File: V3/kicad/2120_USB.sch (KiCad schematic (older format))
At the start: 5 parts, among them J2120 USB_B, J2121 Conn_01x03_Male, U2120 MCP2221AxP

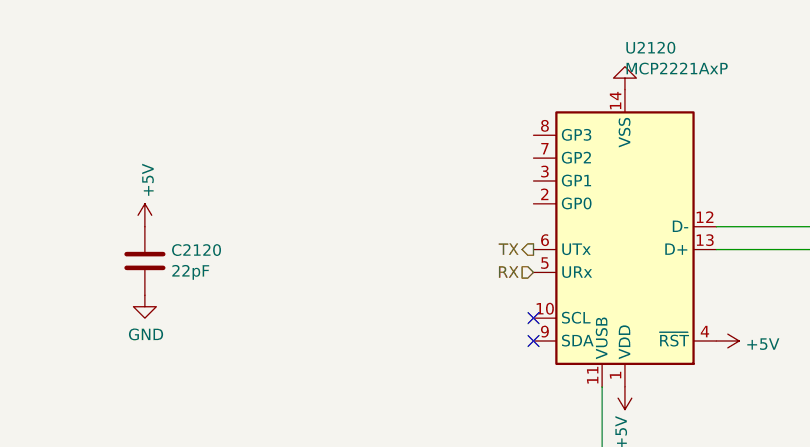
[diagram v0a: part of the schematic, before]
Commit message: Fixed a few USB/UART issues
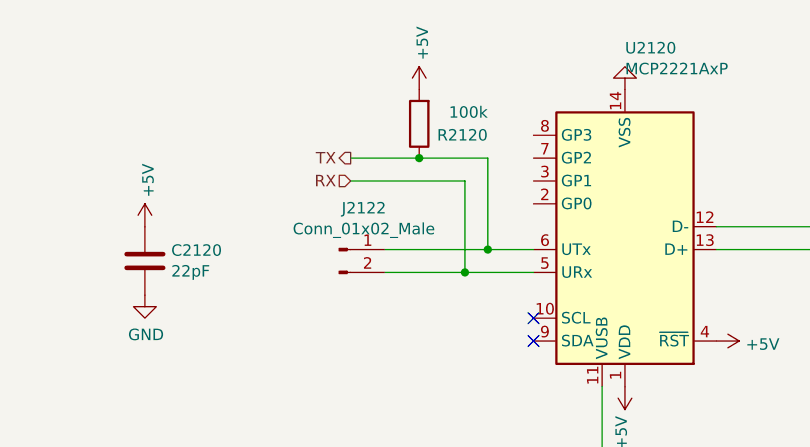
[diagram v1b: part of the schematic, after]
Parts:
- added J2122: Conn_01x02_Male, Connector_PinHeader_2.54mm:PinHeader_1x02_P2.54mm_Vertical, symbol Connector:Conn_01x02_Male
- added R2120: 100k, Resistor_THT:R_Axial_DIN0309_L9.0mm_D3.2mm_P2.54mm_Vertical, symbol Device:R
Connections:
- net +5V: now also R2120.2
- net RX: now also J2122.2 (Pin_2)
- net TX: now also J2122.1 (Pin_1), R2120.1
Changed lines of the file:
@@
 NoConn ~ 4650 4300
 NoConn ~ 4650 4400
-Text HLabel 4650 4000 0    50   Output ~ 0
-TX
-Text HLabel 4650 4100 0    50   Input ~ 0
-RX
 $Comp
 L Connector:Conn_01x03_Male J?
@@
 	1    0    0    -1
 $EndComp
+$Comp
+L Connector:Conn_01x02_Male J2122
+U 1 1 627627D6
+P 3800 4000
+F 0 "J2122" H 3908 4181 50  0000 C CNN
+F 1 "Conn_01x02_Male" H 3908 4090 50  0000 C CNN
+F 2 "Connector_PinHeader_2.54mm:PinHeader_1x02_P2.54mm_Vertical" H 3800 4000 50  0001 C CNN
+F 3 "~" H 3800 4000 50  0001 C CNN
+	1    3800 4000
+	1    0    0    -1
+$EndComp
+Wire Wire Line
+	3850 3600 4150 3600
+Wire Wire Line
+	3850 3700 4350 3700
+$Comp
+L power:+5V #PWR?
+U 1 1 6278A36E
+P 4150 3300
+AR Path="/6191B6A2/61EBDADB/6278A36E" Ref="#PWR?"  Part="1"
+AR Path="/6191B6A2/61EBDADB/62542978/6278A36E" Ref="#PWR0145"  Part="1"
+F 0 "#PWR0145" H 4150 3150 50  0001 C CNN
+F 1 "+5V" V 4165 3428 50  0000 L CNN
+F 2 "" H 4150 3300 50  0001 C CNN
+F 3 "" H 4150 3300 50  0001 C CNN
+	1    4150 3300
+	1    0    0    -1
+$EndComp
+$Comp
+L Device:R R2120
+U 1 1 6278730B
+P 4150 3450
+F 0 "R2120" H 3850 3500 50  0000 L CNN
+F 1 "100k" H 3850 3400 50  0000 L CNN
+F 2 "Resistor_THT:R_Axial_DIN0309_L9.0mm_D3.2mm_P2.54mm_Vertical" V 4080 3450 50  0001 C CNN
+F 3 "~" H 4150 3450 50  0001 C CNN
+	1    4150 3450
+	-1   0    0    1
+$EndComp
+Wire Wire Line
+	4450 3600 4450 4000
+Wire Wire Line
+	4450 4000 4650 4000
+Connection ~ 4450 4000
+Wire Wire Line
+	4450 4000 4000 4000
+Wire Wire Line
+	4650 4100 4350 4100
+Wire Wire Line
+	4000 4100 4350 4100
+Connection ~ 4350 4100
+Wire Wire Line
+	4350 3700 4350 4100
+Text HLabel 3850 3600 0    50   Output ~ 0
+TX
+Text HLabel 3850 3700 0    50   Input ~ 0
+RX
+Connection ~ 4150 3600
+Wire Wire Line
+	4150 3600 4450 3600
 $EndSCHEMATC

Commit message: Still putting final touches on CPU page
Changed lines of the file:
@@
 U 1 1 627627D6
 P 3800 4000
-F 0 "J2122" H 3908 4181 50  0000 C CNN
-F 1 "Conn_01x02_Male" H 3908 4090 50  0000 C CNN
+F 0 "J2122" H 3900 3800 50  0000 C CNN
+F 1 "Conn_01x02_Male" H 3900 3700 50  0000 C CNN
 F 2 "Connector_PinHeader_2.54mm:PinHeader_1x02_P2.54mm_Vertical" H 3800 4000 50  0001 C CNN
 F 3 "~" H 3800 4000 50  0001 C CNN

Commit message: Final checks and DRC
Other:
- note added: "This page has been checked!"
- note removed: "This page has NOT been checked!"
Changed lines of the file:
@@
 Connection ~ 6150 4200
 Text Notes 1250 6500 0    197  ~ 39
-This page has NOT been checked!
+This page has been checked!
 $Comp
 L Device:C C?

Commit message: Design Rule Check
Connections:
- no-connect marks 2 -> 6
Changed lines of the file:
@@
 Wire Wire Line
 	4150 3600 4450 3600
+NoConn ~ 4650 3500
+NoConn ~ 4650 3600
+NoConn ~ 4650 3700
+NoConn ~ 4650 3800
 $EndSCHEMATC

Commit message: just totally redid the whole thing
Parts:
- removed J2121: Conn_01x03_Male, Connector_PinHeader_2.54mm:PinHeader_1x03_P2.54mm_Vertical, symbol Connector:Conn_01x03_Male
- C2120, C2121: footprint Capacitor_THT:C_Rect_L4.0mm_W2.5mm_P2.50mm -> Capacitor_SMD:C_1206_3216Metric
- R2120: footprint Resistor_THT:R_Axial_DIN0309_L9.0mm_D3.2mm_P2.54mm_Vertical -> Resistor_SMD:R_1206_3216Metric
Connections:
- net +5V: now also J2120.1 (VBUS)
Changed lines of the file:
@@
 $Descr A4 11693 8268
 encoding utf-8
-Sheet 9 9
+Sheet 8 8
 Title ""
 Date ""
@@
 L power:+5V #PWR?
 U 1 1 6254C2ED
-P 6150 4200
+P 6350 4200
 AR Path="/6191B6A2/61EBDADB/6254C2ED" Ref="#PWR?"  Part="1"
 AR Path="/6191B6A2/61EBDADB/62542978/6254C2ED" Ref="#PWR0133"  Part="1"
-F 0 "#PWR0133" H 6150 4050 50  0001 C CNN
-F 1 "+5V" V 6165 4328 50  0000 L CNN
-F 2 "" H 6150 4200 50  0001 C CNN
-F 3 "" H 6150 4200 50  0001 C CNN
-	1    6150 4200
+F 0 "#PWR0133" H 6350 4050 50  0001 C CNN
+F 1 "+5V" V 6365 4328 50  0000 L CNN
+F 2 "" H 6350 4200 50  0001 C CNN
+F 3 "" H 6350 4200 50  0001 C CNN
+	1    6350 4200
 	0    -1   -1   0
 $EndComp
@@
 NoConn ~ 4650 4300
 NoConn ~ 4650 4400
-$Comp
-L Connector:Conn_01x03_Male J?
-U 1 1 6254C2E6
-P 6250 4400
-AR Path="/6191B6A2/61EBDADB/6254C2E6" Ref="J?"  Part="1"
-AR Path="/6191B6A2/61EBDADB/62542978/6254C2E6" Ref="J2121"  Part="1"
-F 0 "J2121" V 6358 4589 50  0000 L CNN
-F 1 "Conn_01x03_Male" H 6358 4590 50  0001 C CNN
-F 2 "Connector_PinHeader_2.54mm:PinHeader_1x03_P2.54mm_Vertical" H 6250 4400 50  0001 C CNN
-F 3 "~" H 6250 4400 50  0001 C CNN
-	1    6250 4400
-	0    -1   -1   0
-$EndComp
-Wire Wire Line
-	6150 4200 6250 4200
-Connection ~ 6150 4200
 Text Notes 1250 6500 0    197  ~ 39
 This page has been checked!
@@
 F 0 "C2120" H 3065 4096 50  0000 L CNN
 F 1 "22pF" H 3065 4005 50  0000 L CNN
-F 2 "Capacitor_THT:C_Rect_L4.0mm_W2.5mm_P2.50mm" H 2988 3900 50  0001 C CNN
+F 2 "Capacitor_SMD:C_1206_3216Metric" H 2988 3900 50  0001 C CNN
 F 3 "~" H 2950 4050 50  0001 C CNN
 	1    2950 4050
@@
 F 0 "C2121" H 5065 5146 50  0000 L CNN
 F 1 "22pF" H 5065 5055 50  0000 L CNN
-F 2 "Capacitor_THT:C_Rect_L4.0mm_W2.5mm_P2.50mm" H 4988 4950 50  0001 C CNN
+F 2 "Capacitor_SMD:C_1206_3216Metric" H 4988 4950 50  0001 C CNN
 F 3 "~" H 4950 5100 50  0001 C CNN
 	1    4950 5100
@@
 F 0 "R2120" H 3850 3500 50  0000 L CNN
 F 1 "100k" H 3850 3400 50  0000 L CNN
-F 2 "Resistor_THT:R_Axial_DIN0309_L9.0mm_D3.2mm_P2.54mm_Vertical" V 4080 3450 50  0001 C CNN
+F 2 "Resistor_SMD:R_1206_3216Metric" V 4080 3450 50  0001 C CNN
 F 3 "~" H 4150 3450 50  0001 C CNN
 	1    4150 3450
